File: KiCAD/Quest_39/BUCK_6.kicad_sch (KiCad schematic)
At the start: 32 parts, among them U28 AD626ANZ, U29 INA226, U30 LTM4611EV-PBF, U31 MCP4151-502E/SN

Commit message: Fixed INA226 schem. mistake and further layout work
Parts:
- added C108: 100nF, Capacitor_SMD:C_0603_1608Metric, symbol Device:C
- renumbered C98 to C104, C99 to C105, C100 to C106, C101 to C107, C102 to C109, C103 to C110, C104 to C111, C105 to C112, C106 to C113, C107 to C114, C108 to C115, C109 to C116, C110 to C117, C111 to C118
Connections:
- net +5V: now also C108.1
- net GND: now also C108.2
- net PV_POS: no longer C104.1, C105.1, C106.1, C107.1, R59.2, R61.1, R64.1, U30.A1 (VIN), U30.A2 (VIN), U30.A3 (VIN), U30.A4 (VIN), U30.A5 (VIN), U30.A6 (VIN), U30.B1 (VIN), U30.B2 (VIN), U30.B3 (VIN), U30.B4 (VIN), U30.B5 (VIN), U30.B6 (VIN), U30.C1 (VIN), U30.C2 (VIN), U30.C3 (VIN), U30.C4 (VIN), U30.C5 (VIN), U30.C6 (VIN)
- net Vin-: no longer TP49.1, U28.5 (OUT), U29.8 (Vbus)
- new net: TP49.1, U28.5 (OUT), U29.8 (Vbus)
- new net BUCK_VIN: C104.1, C105.1, C106.1, C107.1, R59.2, R61.1, R64.1, U30.A1 (VIN), U30.A2 (VIN), U30.A3 (VIN), U30.A4 (VIN), U30.A5 (VIN), U30.A6 (VIN), U30.B1 (VIN), U30.B2 (VIN), U30.B3 (VIN), U30.B4 (VIN), U30.B5 (VIN), U30.B6 (VIN), U30.C1 (VIN), U30.C2 (VIN), U30.C3 (VIN), U30.C4 (VIN), U30.C5 (VIN), U30.C6 (VIN)

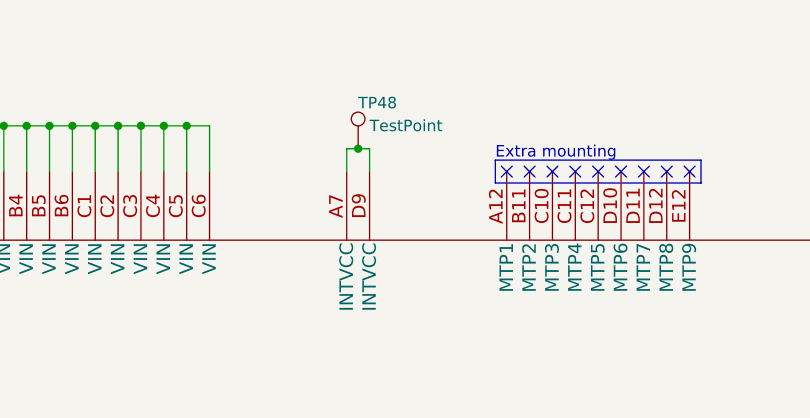
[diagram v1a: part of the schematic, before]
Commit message: Partial wiring of first buck converter section PCB layout
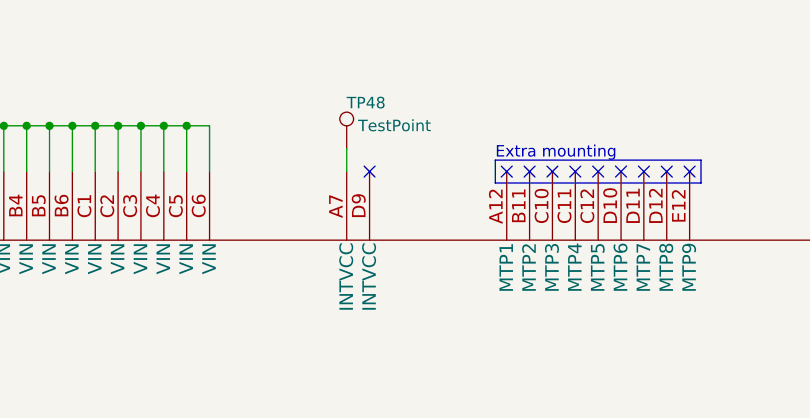
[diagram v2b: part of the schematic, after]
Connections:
- net at TP48.1, U30.A7 (INTVCC): no longer U30.D9 (INTVCC)
- no-connect marks 12 -> 13

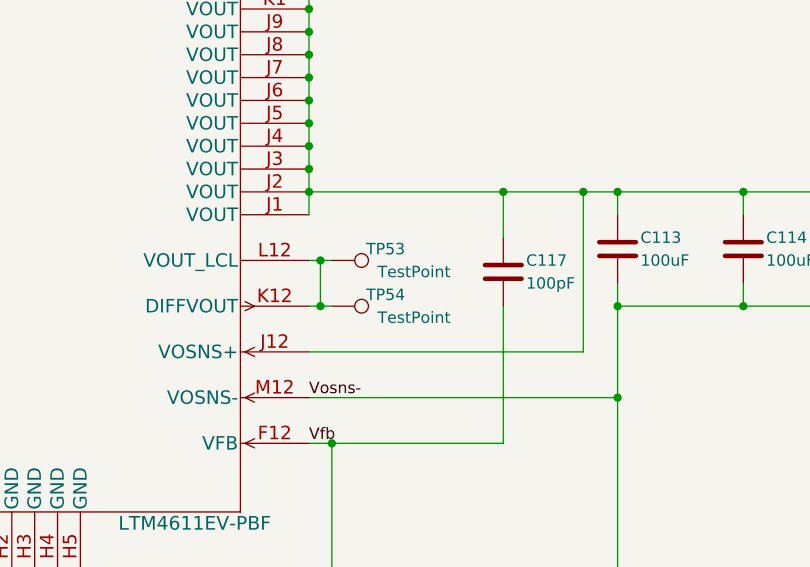
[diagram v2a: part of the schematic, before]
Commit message: Added 3rd buck converter section
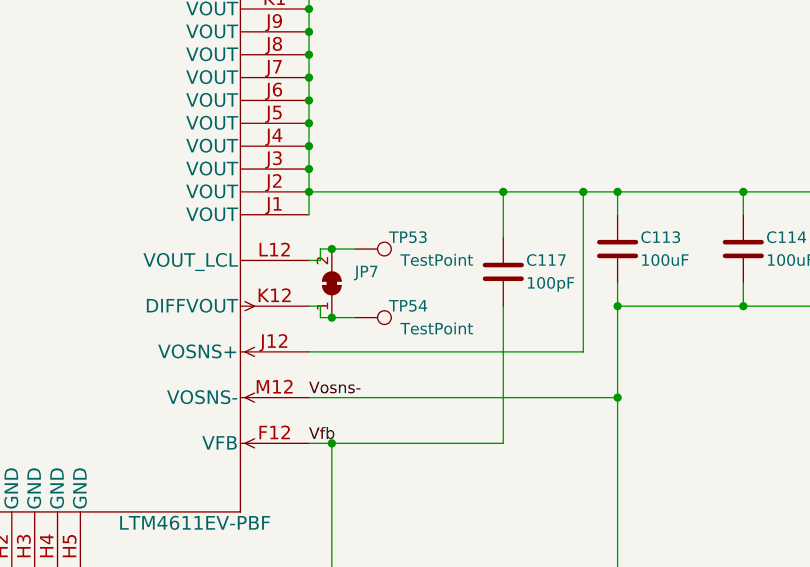
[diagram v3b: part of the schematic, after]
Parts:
- added JP7: SolderJumper_2_Bridged, Jumper:SolderJumper-2_P1.3mm_Bridged_RoundedPad1.0x1.5mm, symbol Jumper:SolderJumper_2_Bridged
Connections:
- net at TP54.1, U30.K12 (DIFFVOUT): now also JP7.1 (A); no longer TP53.1, U30.L12 (VOUT_LCL)
- new net: JP7.2 (B), TP53.1, U30.L12 (VOUT_LCL)
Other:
- moved on the sheet: TP53, TP54

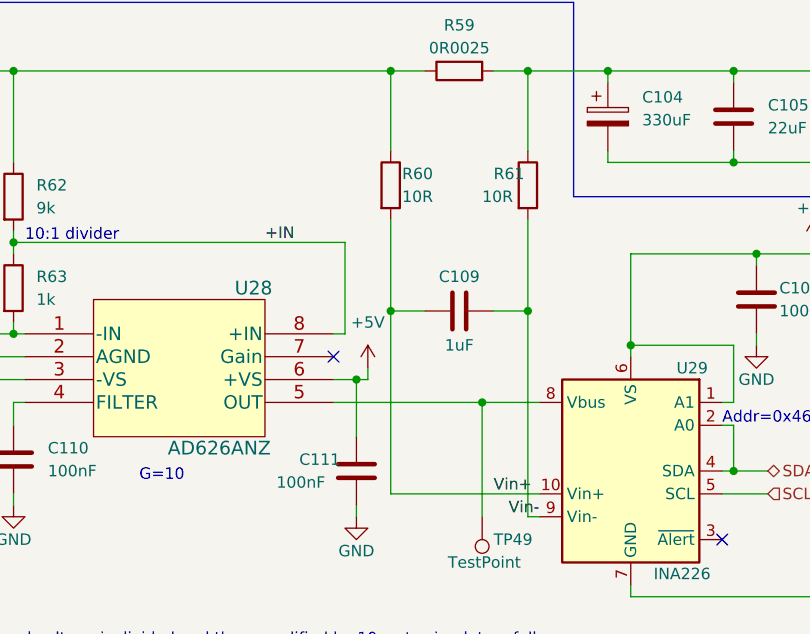
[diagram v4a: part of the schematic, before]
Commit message: Redid layout for the LTM4611EV Buck-converters (Issues with net-assignment to IC pads)
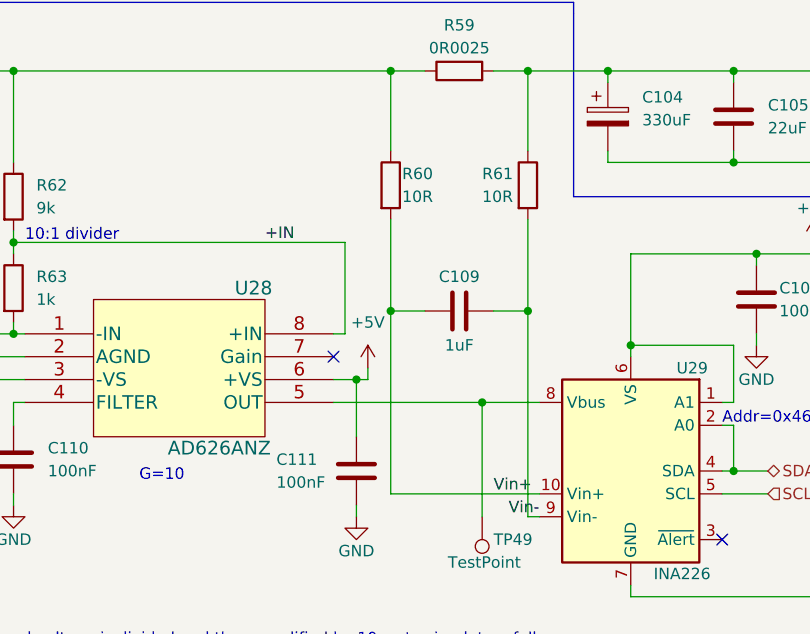
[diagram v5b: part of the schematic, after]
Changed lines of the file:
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@@
   (symbol (lib_id "Device:R") (at 82.55 46.99 0) (unit 1)
     (in_bom yes) (on_board yes)
-    (property "Reference" "R61" (id 0) (at 78.74 45.72 0)
+    (property "Reference" "R61" (id 0) (at 77.47 45.72 0)
       (effects (font (size 1.27 1.27)) (justify left))
     )
@@
   (symbol (lib_id "Device:C") (at 63.5 78.74 0) (unit 1)
     (in_bom yes) (on_board yes)
-    (property "Reference" "C111" (id 0) (at 57.15 77.47 0)
-      (effects (font (size 1.27 1.27)) (justify left))
-    )
+    (property "Reference" "C111" (id 0) (at 54.61 77.47 0)
+      (effects (font (size 1.27 1.27)) (justify left))
+    )

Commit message: Added all the SolidWorks files, edited README
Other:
- title: (none) -> BUCK_6
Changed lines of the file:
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@@
 (kicad_sch (version 20211123) (generator eeschema)
   (paper "A3")
+  (title_block
+    (title "BUCK_6")
+    (date "2023-01-31")
+    (rev "1.0")
+  )
   (junction (at 21.59 68.58) (diameter 0) (color 0 0 0 0)
   )
